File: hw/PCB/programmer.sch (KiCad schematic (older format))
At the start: 2 parts, among them J2 Programmer

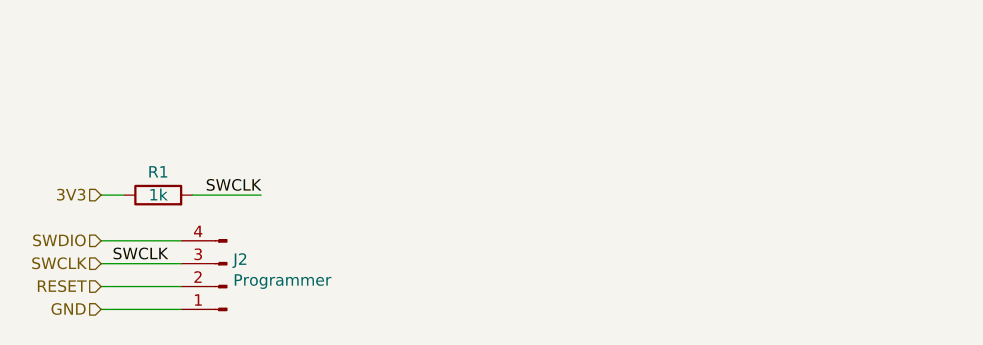
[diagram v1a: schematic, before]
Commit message: Added a footprint library for a micro SD card. Updated the schematic. Replaced the SAMD21G with the SAMD21E (32 pin variant). Added a data logger and a reset button.
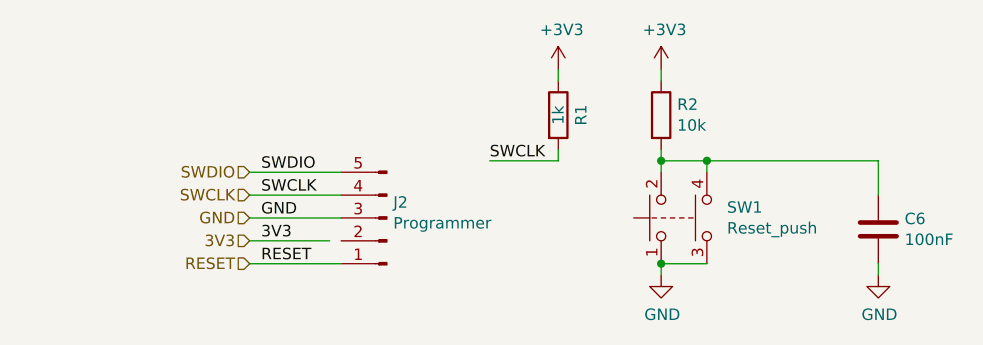
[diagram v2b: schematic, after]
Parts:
- removed J2: Programmer, Connector_PinHeader_2.54mm:PinHeader_1x04_P2.54mm_Vertical, symbol Connector:Conn_01x04_Male
- added C6: 100nF, symbol Device:C
- added J2: Programmer, symbol Connector:Conn_01x05_Male
- added R2: 10k, symbol Device:R
- added SW1: Reset_push, symbol Switch:SW_Push_Dual
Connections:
- net labels added: +3V3
- wire segments 6 -> 18
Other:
- moved on the sheet: R1
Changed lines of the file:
@@
 $Descr A4 11693 8268
 encoding utf-8
-Sheet 5 5
+Sheet 5 6
 Title ""
 Date ""
@@
 Comment4 ""
 $EndDescr
-$Comp
-L Connector:Conn_01x04_Male J2
-U 1 1 5BFFAA36
-P 4750 3100
-F 0 "J2" H 4722 2982 50  0000 R CNN
-F 1 "Programmer" H 4722 3073 50  0000 R CNN
-F 2 "Connector_PinHeader_2.54mm:PinHeader_1x04_P2.54mm_Vertical" H 4750 3100 50  0001 C CNN
-F 3 "~" H 4750 3100 50  0001 C CNN
-	1    4750 3100
-	-1   0    0    1
-$EndComp
-Text HLabel 4200 2700 0    50   Input ~ 0
+Text HLabel 4850 2900 0    50   Input ~ 0
 3V3
-Text HLabel 4200 2900 0    50   Input ~ 0
+Text HLabel 4850 2600 0    50   Input ~ 0
 SWDIO
-Text HLabel 4200 3000 0    50   Input ~ 0
+Text HLabel 4850 2700 0    50   Input ~ 0
 SWCLK
-Text HLabel 4200 3100 0    50   Input ~ 0
+Text HLabel 4850 3000 0    50   Input ~ 0
 RESET
-Text HLabel 4200 3200 0    50   Input ~ 0
+Text HLabel 4850 2800 0    50   Input ~ 0
 GND
 $Comp
 L Device:R R1
 U 1 1 5BFFC4E5
-P 4450 2700
-F 0 "R1" V 4550 2700 50  0000 C CNN
-F 1 "1k" V 4450 2700 50  0000 C CNN
-F 2 "Resistor_SMD:R_0603_1608Metric_Pad1.05x0.95mm_HandSolder" V 4380 2700 50  0001 C CNN
-F 3 "~" H 4450 2700 50  0001 C CNN
-	1    4450 2700
+P 6200 2350
+F 0 "R1" V 6300 2350 50  0000 C CNN
+F 1 "1k" V 6200 2350 50  0000 C CNN
+F 2 "Resistor_SMD:R_0603_1608Metric_Pad1.05x0.95mm_HandSolder" V 6130 2350 50  0001 C CNN
+F 3 "~" H 6200 2350 50  0001 C CNN
+	1    6200 2350
+	1    0    0    -1
+$EndComp
+Text Label 5900 2550 0    50   ~ 0
+SWCLK
+Text Label 4900 2700 0    50   ~ 0
+SWCLK
+$Comp
+L Connector:Conn_01x05_Male J2
+U 1 1 5D1D6EC1
+P 5450 2800
+F 0 "J2" H 5422 2732 50  0000 R CNN
+F 1 "Programmer" H 5422 2823 50  0000 R CNN
+F 2 "" H 5450 2800 50  0001 C CNN
+F 3 "~" H 5450 2800 50  0001 C CNN
+	1    5450 2800
+	-1   0    0    1
+$EndComp
+Text Label 4900 3000 0    50   ~ 0
+RESET
+$Comp
+L Device:C C6
+U 1 1 5D1DAA3D
+P 7600 2850
+F 0 "C6" H 7715 2896 50  0000 L CNN
+F 1 "100nF" H 7715 2805 50  0000 L CNN
+F 2 "" H 7638 2700 50  0001 C CNN
+F 3 "~" H 7600 2850 50  0001 C CNN
+	1    7600 2850
+	1    0    0    -1
+$EndComp
+Wire Wire Line
+	6650 2550 6850 2550
+Wire Wire Line
+	6650 2500 6650 2550
+Wire Wire Line
+	7600 3000 7600 3050
+$Comp
+L Switch:SW_Push_Dual SW1
+U 1 1 5D1E1E72
+P 6650 2800
+F 0 "SW1" V 6696 2512 50  0000 R CNN
+F 1 "Reset_push" V 6605 2512 50  0000 R CNN
+F 2 "" H 6650 3000 50  0001 C CNN
+F 3 "~" H 6650 3000 50  0001 C CNN
+	1    6650 2800
 	0    -1   -1   0
 $EndComp
-Text Label 4900 2700 2    50   ~ 0
-SWCLK
 Wire Wire Line
-	4900 2700 4600 2700
+	6650 3000 6850 3000
+Connection ~ 6650 3000
 Wire Wire Line
-	4300 2700 4200 2700
-Text Label 4250 3000 0    50   ~ 0
-SWCLK
+	6650 3000 6650 3050
+$Comp
+L Device:R R2
+U 1 1 5D1DB464
+P 6650 2350
+F 0 "R2" H 6720 2396 50  0000 L CNN
+F 1 "10k" H 6720 2305 50  0000 L CNN
+F 2 "" V 6580 2350 50  0001 C CNN
+F 3 "~" H 6650 2350 50  0001 C CNN
+	1    6650 2350
+	1    0    0    -1
+$EndComp
 Wire Wire Line
-	4550 2900 4200 2900
+	7600 2550 7600 2700
+Connection ~ 6850 2550
+Connection ~ 6650 2550
 Wire Wire Line
-	4200 3000 4550 3000
+	6850 2550 7600 2550
+$Comp
+L power:GND #PWR?
+U 1 1 5D1DAC80
+P 6650 3050
+F 0 "#PWR?" H 6650 2800 50  0001 C CNN
+F 1 "GND" H 6655 2877 50  0000 C CNN
+F 2 "" H 6650 3050 50  0001 C CNN
+F 3 "" H 6650 3050 50  0001 C CNN
+	1    6650 3050
+	1    0    0    -1
+$EndComp
+$Comp
+L power:GND #PWR?
+U 1 1 5D1DFA15
+P 7600 3050
+F 0 "#PWR?" H 7600 2800 50  0001 C CNN
+F 1 "GND" H 7605 2877 50  0000 C CNN
+F 2 "" H 7600 3050 50  0001 C CNN
+F 3 "" H 7600 3050 50  0001 C CNN
+	1    7600 3050
+	1    0    0    -1
+$EndComp
+$Comp
+L power:+3V3 #PWR?
+U 1 1 5D1DAF69
+P 6650 2150
+F 0 "#PWR?" H 6650 2000 50  0001 C CNN
+F 1 "+3V3" H 6665 2323 50  0000 C CNN
+F 2 "" H 6650 2150 50  0001 C CNN
+F 3 "" H 6650 2150 50  0001 C CNN
+	1    6650 2150
+	1    0    0    -1
+$EndComp
 Wire Wire Line
-	4550 3100 4200 3100
+	6650 2150 6650 2200
 Wire Wire Line
-	4200 3200 4550 3200
+	6650 2550 6650 2600
+Wire Wire Line
+	6850 2600 6850 2550
+$Comp
+L power:+3V3 #PWR?
+U 1 1 5D1EBFB7
+P 6200 2150
+F 0 "#PWR?" H 6200 2000 50  0001 C CNN
+F 1 "+3V3" H 6215 2323 50  0000 C CNN
+F 2 "" H 6200 2150 50  0001 C CNN
+F 3 "" H 6200 2150 50  0001 C CNN
+	1    6200 2150
+	1    0    0    -1
+$EndComp
+Text Label 4900 2600 0    50   ~ 0
+SWDIO
+Text Label 4900 2800 0    50   ~ 0
+GND
+Text Label 4900 2900 0    50   ~ 0
+3V3
+Wire Wire Line
+	4850 2600 5250 2600
+Wire Wire Line
+	4850 2700 5250 2700
+Wire Wire Line
+	4850 2800 5250 2800
+Wire Wire Line
+	5200 2900 4850 2900
+Wire Wire Line
+	4850 3000 5250 3000
+Wire Wire Line
+	6200 2200 6200 2150
+Wire Wire Line
+	6200 2500 6200 2550
+Wire Wire Line
+	6200 2550 5900 2550
 $EndSCHEMATC

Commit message: Started the new design of the PCB's layout.
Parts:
- C6: footprint (none) -> Capacitor_SMD:C_0603_1608Metric_Pad1.05x0.95mm_HandSolder
- J2: footprint (none) -> Connector_PinHeader_2.54mm:PinHeader_1x05_P2.54mm_Vertical
- R2: footprint (none) -> Resistor_SMD:R_0603_1608Metric_Pad1.05x0.95mm_HandSolder
- SW1: footprint (none) -> Button_Switch_THT:SW_TH_Tactile_Omron_B3F-10xx
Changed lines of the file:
@@
 F 0 "J2" H 5422 2732 50  0000 R CNN
 F 1 "Programmer" H 5422 2823 50  0000 R CNN
-F 2 "" H 5450 2800 50  0001 C CNN
+F 2 "Connector_PinHeader_2.54mm:PinHeader_1x05_P2.54mm_Vertical" H 5450 2800 50  0001 C CNN
 F 3 "~" H 5450 2800 50  0001 C CNN
 	1    5450 2800
@@
 F 0 "C6" H 7715 2896 50  0000 L CNN
 F 1 "100nF" H 7715 2805 50  0000 L CNN
-F 2 "" H 7638 2700 50  0001 C CNN
+F 2 "Capacitor_SMD:C_0603_1608Metric_Pad1.05x0.95mm_HandSolder" H 7638 2700 50  0001 C CNN
 F 3 "~" H 7600 2850 50  0001 C CNN
 	1    7600 2850
@@
 F 0 "SW1" V 6696 2512 50  0000 R CNN
 F 1 "Reset_push" V 6605 2512 50  0000 R CNN
-F 2 "" H 6650 3000 50  0001 C CNN
+F 2 "Button_Switch_THT:SW_TH_Tactile_Omron_B3F-10xx" H 6650 3000 50  0001 C CNN
 F 3 "~" H 6650 3000 50  0001 C CNN
 	1    6650 2800
@@
 U 1 1 5D1DB464
 P 6650 2350
-F 0 "R2" H 6720 2396 50  0000 L CNN
-F 1 "10k" H 6720 2305 50  0000 L CNN
-F 2 "" V 6580 2350 50  0001 C CNN
+F 0 "R2" V 6750 2300 50  0000 L CNN
+F 1 "10k" V 6650 2300 50  0000 L CNN
+F 2 "Resistor_SMD:R_0603_1608Metric_Pad1.05x0.95mm_HandSolder" V 6580 2350 50  0001 C CNN
 F 3 "~" H 6650 2350 50  0001 C CNN
 	1    6650 2350
@@
 	6850 2550 7600 2550
 $Comp
-L power:GND #PWR?
+L power:GND #PWR0120
 U 1 1 5D1DAC80
 P 6650 3050
-F 0 "#PWR?" H 6650 2800 50  0001 C CNN
+F 0 "#PWR0120" H 6650 2800 50  0001 C CNN
 F 1 "GND" H 6655 2877 50  0000 C CNN
 F 2 "" H 6650 3050 50  0001 C CNN
@@
 $EndComp
 $Comp
-L power:GND #PWR?
+L power:GND #PWR0121
 U 1 1 5D1DFA15
 P 7600 3050
-F 0 "#PWR?" H 7600 2800 50  0001 C CNN
+F 0 "#PWR0121" H 7600 2800 50  0001 C CNN
 F 1 "GND" H 7605 2877 50  0000 C CNN
 F 2 "" H 7600 3050 50  0001 C CNN
@@
 $EndComp
 $Comp
-L power:+3V3 #PWR?
+L power:+3V3 #PWR0122
 U 1 1 5D1DAF69
 P 6650 2150
-F 0 "#PWR?" H 6650 2000 50  0001 C CNN
+F 0 "#PWR0122" H 6650 2000 50  0001 C CNN
 F 1 "+3V3" H 6665 2323 50  0000 C CNN
 F 2 "" H 6650 2150 50  0001 C CNN
@@
 	6850 2600 6850 2550
 $Comp
-L power:+3V3 #PWR?
+L power:+3V3 #PWR0123
 U 1 1 5D1EBFB7
 P 6200 2150
-F 0 "#PWR?" H 6200 2000 50  0001 C CNN
+F 0 "#PWR0123" H 6200 2000 50  0001 C CNN
 F 1 "+3V3" H 6215 2323 50  0000 C CNN
 F 2 "" H 6200 2150 50  0001 C CNN
@@
 	4850 2800 5250 2800
 Wire Wire Line
-	5200 2900 4850 2900
-Wire Wire Line
 	4850 3000 5250 3000
 Wire Wire Line
@@
 Wire Wire Line
 	6200 2550 5900 2550
+Wire Wire Line
+	4850 2900 5250 2900
+Text Label 6650 2550 0    50   ~ 0
+RESET
 $EndSCHEMATC
